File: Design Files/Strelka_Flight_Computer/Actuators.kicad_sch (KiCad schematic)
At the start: 0 parts

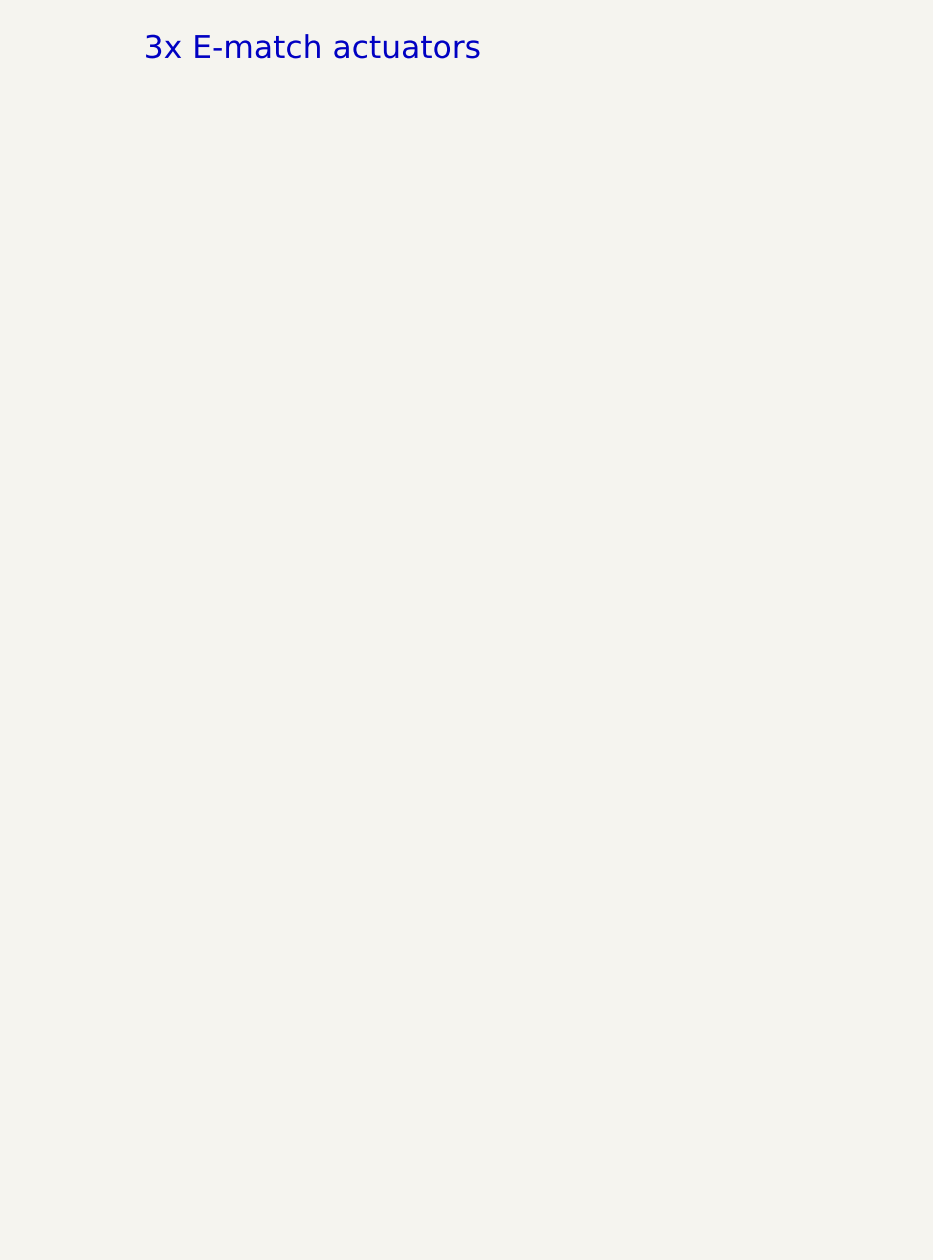
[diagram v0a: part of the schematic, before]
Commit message: Added sensors
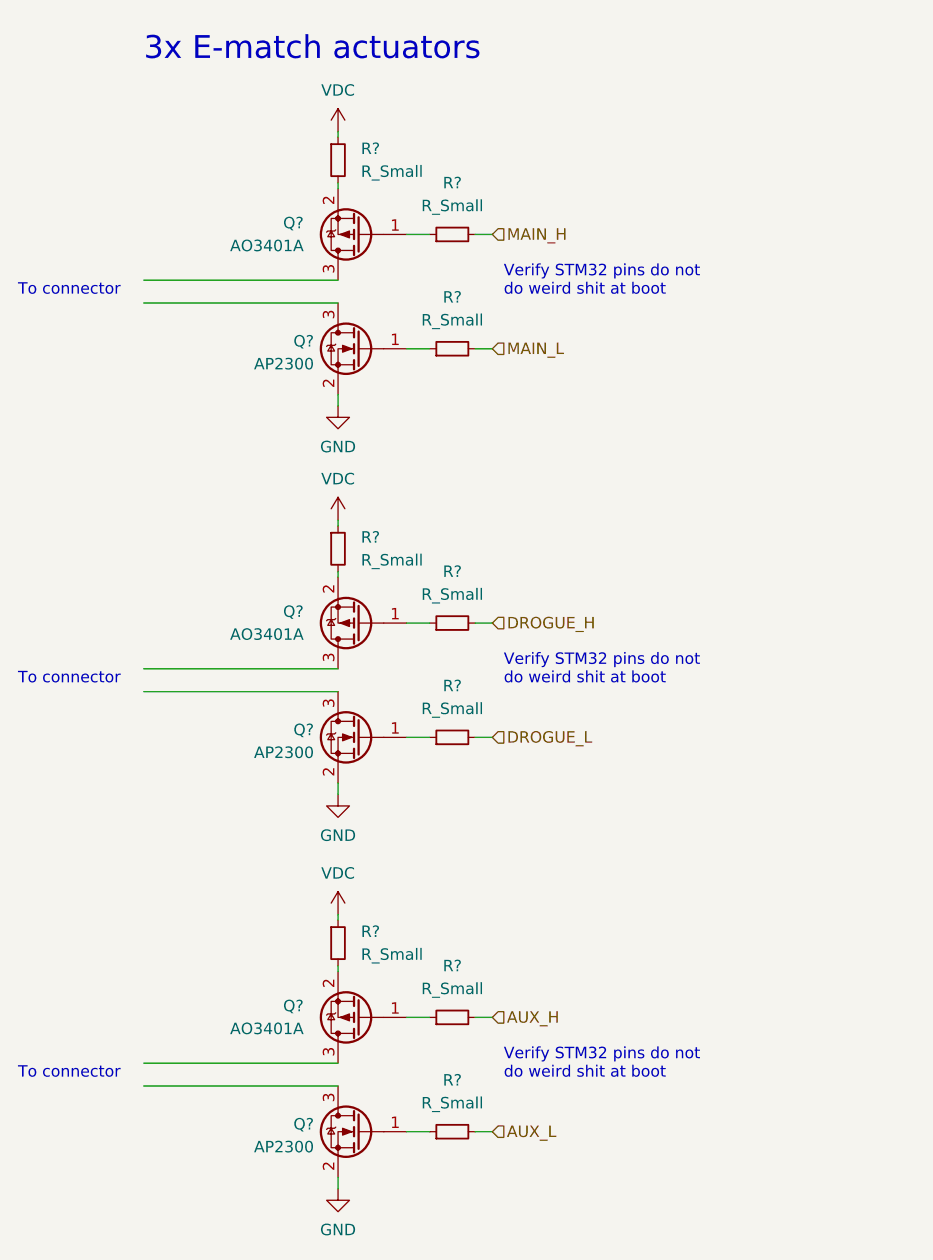
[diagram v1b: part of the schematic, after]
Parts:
- added Q? (x3): AO3401A, Package_TO_SOT_SMD:SOT-23, symbol Transistor_FET:AO3401A
- added Q? (x3): AP2300, Package_TO_SOT_SMD:SOT-23, symbol Transistor_FET:2N7002E
- added R? (x9): R_Small, symbol Device:R_Small
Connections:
- new net: Q?.1 (G), R?.1 (x6)
- new net: Q?.2 (S), R?.2 (x3)
- new net AUX_H: R?.2
- new net AUX_L: R?.2
- new net DROGUE_H: R?.2
- new net DROGUE_L: R?.2
- new net GND: Q?.2 (S), Q?.2 (S), Q?.2 (S)
- new net MAIN_H: R?.2
- new net MAIN_L: R?.2
- new net VDC: R?.1, R?.1, R?.1
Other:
- note added: "To connector"
- note added: "Verify STM32 pins do not do weird shit at boot"

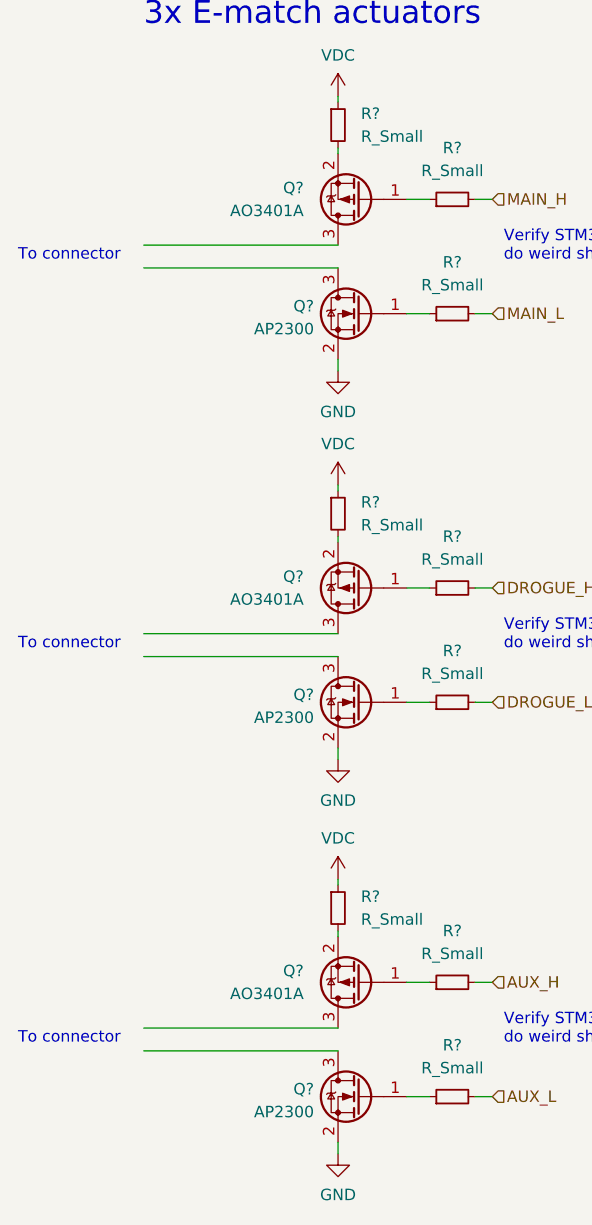
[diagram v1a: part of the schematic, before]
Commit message: Added BMX055
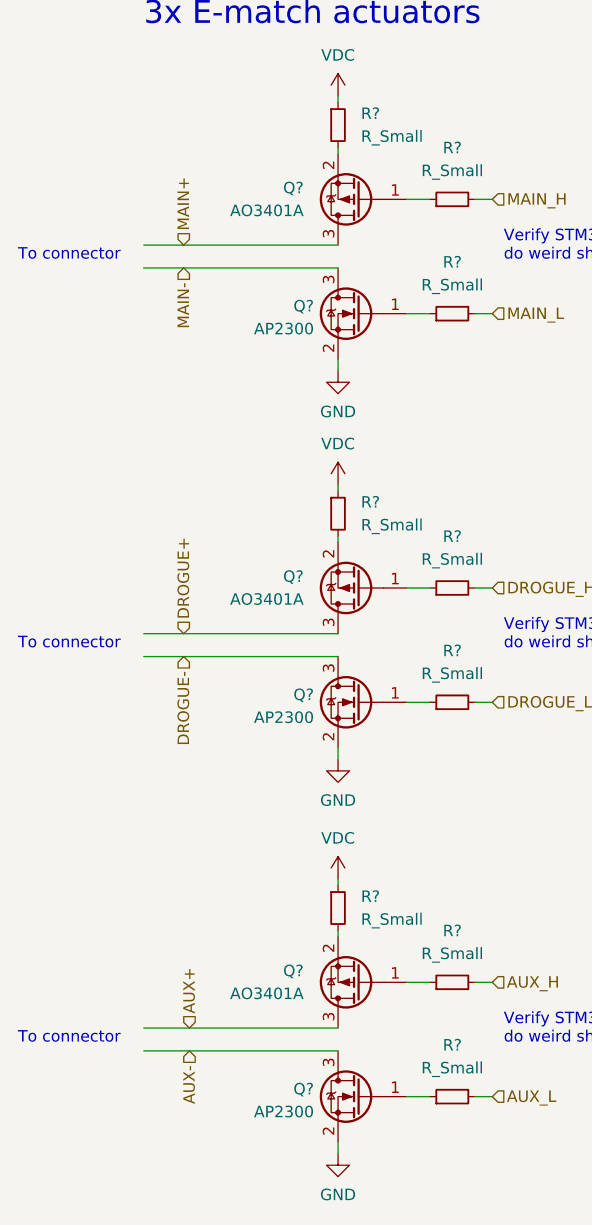
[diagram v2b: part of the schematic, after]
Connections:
- net MAIN+: now reaches Q?.3 (D)
- net AUX+: now reaches Q?.3 (D)
- net DROGUE-: now reaches Q?.3 (D)
- net DROGUE+: now reaches Q?.3 (D)
- net AUX-: now reaches Q?.3 (D)
- net MAIN-: now reaches Q?.3 (D)
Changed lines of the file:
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@@
     (effects (font (size 1.27 1.27)) (justify left bottom))
+  )
+  (hierarchical_label "MAIN-" (shape input) (at 50.165 71.755 270)
+    (effects (font (size 1.27 1.27)) (justify right))
   )
   (hierarchical_label "DROGUE_H" (shape input) (at 84.455 107.315 0)
@@
     (effects (font (size 1.27 1.27)) (justify left))
   )
+  (hierarchical_label "AUX-" (shape input) (at 50.8 158.75 270)
+    (effects (font (size 1.27 1.27)) (justify right))
+  )
   (hierarchical_label "DROGUE_L" (shape input) (at 84.455 120.015 0)
+    (effects (font (size 1.27 1.27)) (justify left))
+  )
+  (hierarchical_label "MAIN+" (shape input) (at 50.165 69.215 90)
+    (effects (font (size 1.27 1.27)) (justify left))
+  )
+  (hierarchical_label "AUX+" (shape input) (at 50.8 156.21 90)
     (effects (font (size 1.27 1.27)) (justify left))
   )
   (hierarchical_label "AUX_L" (shape input) (at 84.455 163.83 0)
     (effects (font (size 1.27 1.27)) (justify left))
+  )
+  (hierarchical_label "DROGUE-" (shape input) (at 50.165 114.935 270)
+    (effects (font (size 1.27 1.27)) (justify right))
   )
   (hierarchical_label "MAIN_H" (shape input) (at 84.455 64.135 0)
@@
     (effects (font (size 1.27 1.27)) (justify left))
   )
+  (hierarchical_label "DROGUE+" (shape input) (at 50.165 112.395 90)
+    (effects (font (size 1.27 1.27)) (justify left))
+  )
